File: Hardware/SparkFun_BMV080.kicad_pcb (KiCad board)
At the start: 2 copper layers, 24.1 x 12.7 mm, 54 parts, among them J1 Qwiic_RA, J2 Conn_01x07, U1 BMV080

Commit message: Changed C5 from DNP to populated
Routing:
- net 3.3V: track 48.2 -> 47.7 mm
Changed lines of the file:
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@@
 		)
 		(group ""
-			(members "0323bbcb-9db1-4550-bdcf-c58307372e8a" "129c8a7c-96b1-4d77-be27-7c0a68eae82b"
-				"17066dd4-91f0-4b2c-90e9-9da69e5faaa6" "1943d318-2756-45dc-b198-7f49738af2c3"
-				"3f605292-b843-4d37-babf-3784242fe08f" "4f4c8642-4329-4bf1-b3ef-893e8dab323c"
-				"57365592-8080-47cf-8e00-2132c18cfec5" "5d47b60e-56bd-45d7-bb0d-a27f9c249cd9"
-				"7191a7ac-3cfd-46b6-b47c-109da5e373e4" "743e579a-8922-4b10-a70a-2bff2a61b4e9"
-				"8350fa8f-af59-4aa9-b07d-7af58feef8e6" "99e0e99d-677b-4fb4-b25c-acb5b0a82601"
-				"9f4f398a-88a8-47ff-bd15-fe353347f26e" "adeaf1fb-c8a8-495c-b3dc-061e1177fc19"
-				"c20d4249-b260-447a-a5e6-acf935c38c30" "cd680a11-ecdf-470c-832d-11c97486f1ce"
-				"d777cdd7-b0db-4b6c-9eb7-9efd6433ac26" "e269340a-8f81-4c65-8b68-691e03761d3e"
-				"f43b7801-056e-4cbc-bdcf-bace62f3a128" "f48c44af-afb6-4a1e-9611-99fc4c60bd91"
-				"f6a77c4c-a699-4998-b09a-588a7a439803" "f8e37a14-ad18-4cdf-afa0-56f7ebb95e30"
-				"f9167eab-9848-4063-82ef-cf8f1aa0283d" "fe6070ae-ec9c-4269-b79c-fb7439431384"
+			(members "0ceba5bc-189c-4eae-8833-ca9dbc079d37" "1f663b43-5c1f-47e9-9c2b-0e138af4ceb2"
+				"35ecef30-701a-4ae0-abb4-b91e4a9bb35f" "4c3070f8-7595-4885-a99a-a6facd63b4d7"
+				"5acd4afe-5e46-4f77-8c4f-4d508bdab7df" "61c7252d-1063-4566-999f-4fc0c4eafa67"
+				"6407c94d-d9f4-4163-83dc-a27446e726f8" "711f668a-bbce-4460-92d5-2e2cb9263932"
+				"86f05a87-cb46-4ce1-99ac-246c7caf3355" "993f312a-53b4-4398-a6b3-1f8ffd14df01"
+				"ae4bcca0-e3f6-4d88-8f8d-e36f1c271b57" "ae4bce81-2b73-4186-9c70-5910d9db9cd7"
+				"af736b6d-5ec5-45a8-b9f0-5d125bc51396" "b1867b9a-aa29-47b2-84da-97c96f2a49b8"
+				"b66097e4-f0a4-4951-b7fc-f9bdb9b19a9e" "c71cbb7c-1523-4b6d-8205-3119d83c7f20"
+				"dcffac79-e62a-421f-9400-1164a284a8d9" "e88fcd85-46ed-4386-a12e-f83662d1dc38"
+				"ecad0877-a816-471d-b628-6088fbfe1e93" "f0717b40-129c-4219-b55f-f7d5f907be79"
+				"f15de511-9ecc-4bba-8d54-4c130d252e85" "f48ce54b-3d15-48d6-96cb-7c2bb2d5acba"
+				"f602eccc-5aa0-4869-a675-a465a2e67a34" "f780c958-a8ac-4002-8a30-fe8cb3588660"
 			)
 		)
 		(group ""
-			(members "3720748d-96f4-44c1-930f-83de2de9e6e6" "3f3fba18-211e-41a3-ba51-976b2923ebd1"
-				"48b4bfa4-e4f8-4cee-8010-c9c6888a8f20" "4ed068ba-5eca-41cd-886a-1229b8814574"
-				"542eba73-4fbb-468b-acee-2bdb3667f254" "6734b2cc-4870-4695-8d09-9d5a7687712e"
-				"6bd0c4f7-2192-41be-8adc-e0c41a3e553a" "93fcdc44-fb1b-4a33-b65b-43d007b5f669"
-				"9548979e-7292-4bed-8904-9b678ba7e0bb" "a480d734-605c-46e8-9c6a-b63f6f2b9b0b"
-				"aa4fac25-a87d-4ceb-99bc-9275ae9cb340" "bcd9040b-70e0-4c06-96e3-043c244d4851"
-				"de0a1da5-8957-4ae4-a6fe-f0af63f92c79" "f6420fb9-895e-4033-a284-81064fd5bd43"
+			(members "0335be06-102d-4263-bab1-12667eda6e8b" "38c72f74-21d1-425c-b6e8-509a0f78b6f3"
+				"3e9c3e0c-8359-4605-b76b-e8b7b21f3528" "505c8171-6575-45b8-8b41-329f054488d6"
+				"67fac45c-d807-45a9-bd04-f7a23e01c00d" "899ac419-171b-4f1c-b566-96660c695bdc"
+				"a2e41c72-f8ca-4b1a-82d9-f3002f2ddce2" "a6349dca-2aff-4e1a-b036-bd771e3eb8f8"
+				"bf23a2b1-279c-4095-b615-8f9de98552e9" "d26edaaf-7e9e-4d26-a137-f035ce0b2bc4"
+				"d627d596-f0cd-4127-9f8a-afefe62d29bf" "e23e056e-79b9-4709-94fd-23d215b02856"
+				"e99c97d1-8692-4be9-aaab-415d2e226c84" "fa415e96-26ef-4dcb-bd23-2b3b71b8cb64"
 			)
 		)
 		(model "${KIPRJMOD}/BMV080.3dshapes/BMV080_Sensor_and_FPC_Connector.step"
 			(offset
-				(xyz -0.35 -23.2 2)
+				(xyz -0.35 -23.15 1.97)
 			)
 			(scale
@@
 		(tags "SparkFun capacitor")
 		(property "Reference" "C5"
-			(at 0 1.43 90)
+			(at 0 1.43 -90)
 			(layer "B.Fab")
 			(effects
@@
 		)
 		(property "Value" "10uF"
-			(at 0 -1.43 90)
+			(at 0 -1.43 -90)
 			(layer "B.Fab")
 			(effects
@@
 		(sheetname "Root")
 		(sheetfile "SparkFun_BMV080.kicad_sch")
-		(attr smd dnp)
-		(fp_line
-			(start 0.14058 -0.51)
-			(end -0.14058 -0.51)
-			(stroke
-				(width 0.12)
-				(type solid)
-			)
-			(layer "B.SilkS")
-		)
-		(fp_line
-			(start 0.14058 0.51)
-			(end -0.14058 0.51)
+		(attr smd)
+		(fp_rect
+			(start -1.337 0.598)
+			(end 1.336 -0.586)
 			(stroke
-				(width 0.12)
-				(type solid)
+				(width 0.1)
+				(type default)
 			)
+			(fill none)
 			(layer "B.SilkS")
 		)
@@
 		)
 		(height 11.43)
-		(gr_text "950 mils"
+		(gr_text "24.13 mm"
 			(at 128.905 77.59 0)
 			(layer "Dwgs.User")
@@
 		)
 		(height -8.94)
-		(gr_text "500.00 mils"
+		(gr_text "12.70 mm"
 			(at 107.77 106.58 90)
 			(layer "Dwgs.User")
@@
 		)
 		(height 2.53)
-		(gr_text "60 mils"
+		(gr_text "1.52 mm"
 			(at 144.73 88.82 90)
 			(layer "Dwgs.User")
@@
 		)
 		(height 12.17)
-		(gr_text "179.921 mils"
+		(gr_text "4.57 mm"
 			(at 152.146 90.678 90)
 			(layer "Dwgs.User")
@@
 		(height -6.785)
 		(orientation 1)
-		(gr_text "75.000 mils"
+		(gr_text "1.905 mm"
 			(at 114.42 106.93 90)
 			(layer "Dwgs.User")
@@
 		(height 6.77)
 		(orientation 1)
-		(gr_text "171.1417 mils"
+		(gr_text "4.3470 mm"
 			(at 147.8 85.53 90)
 			(layer "Dwgs.User")
@@
 		(height 4.145)
 		(orientation 0)
-		(gr_text "100.2 mils"
+		(gr_text "2.5 mm"
 			(at 127.15 105.22 0)
 			(layer "Dwgs.User")
@@
 		(height -10.61)
 		(orientation 1)
-		(gr_text "250.00 mils"
+		(gr_text "6.35 mm"
 			(at 111.31 106.39 90)
 			(layer "Dwgs.User")
@@
 		(height 9.99)
 		(orientation 0)
-		(gr_text "175.000 mils"
+		(gr_text "4.445 mm"
 			(at 125.02 112.85 0)
 			(layer "Dwgs.User")
@@
 		(height 10.22)
 		(orientation 0)
-		(gr_text "175.197 mils"
+		(gr_text "4.450 mm"
 			(at 144.88 112.98 0)
 			(layer "Dwgs.User")
@@
 		(height -7.874)
 		(orientation 0)
-		(gr_text "912.2 mils"
+		(gr_text "23.17 mm"
 			(at 128.425 81.146 0)
 			(layer "Dwgs.User")
@@
 		(height -8.927)
 		(orientation 0)
-		(gr_text "124.843 mils"
+		(gr_text "3.171 mm"
 			(at 133.49 85.41 0)
 			(layer "Dwgs.User")
@@
 	)
 	(segment
-		(start 130.81 101.6)
-		(end 130.81 101.05)
-		(width 0.2032)
-		(layer "F.Cu")
-		(net 10)
-	)
-	(segment
 		(start 119.285 94.28)
 		(end 118.32 94.28)
@@
 		(min_thickness 0.254)
 		(filled_areas_thickness no)
-		(fill
+		(fill yes
 			(thermal_gap 0.3048)
 			(thermal_bridge_width 0.3048)

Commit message: ordering instructions updated to RED
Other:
- board text added: "Solder Mask: Red"
- board text removed: "Solder Mask: Black"
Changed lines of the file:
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@@
 		)
 	)
-	(gr_text "Solder Mask: Black"
+	(gr_text "Solder Mask: Red"
 		(at 220.3 172.32 0)
 		(layer "F.Fab")

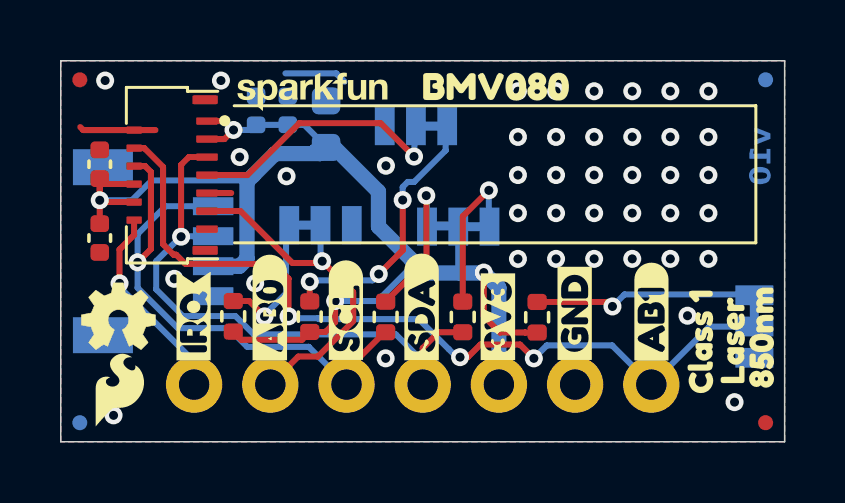
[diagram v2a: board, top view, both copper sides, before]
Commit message: library work
-moved bmv080 sensor symbol and footprint to sparkfun libraries with pending PR.
-updated symbol and footprints in kicad design files
-note, the sensor itself and the FPC connector are now separate things. The BMV080 has an "outline" footprint that is placed at the same origin point as the sensor (and includes the 3d model of the sensor itself)
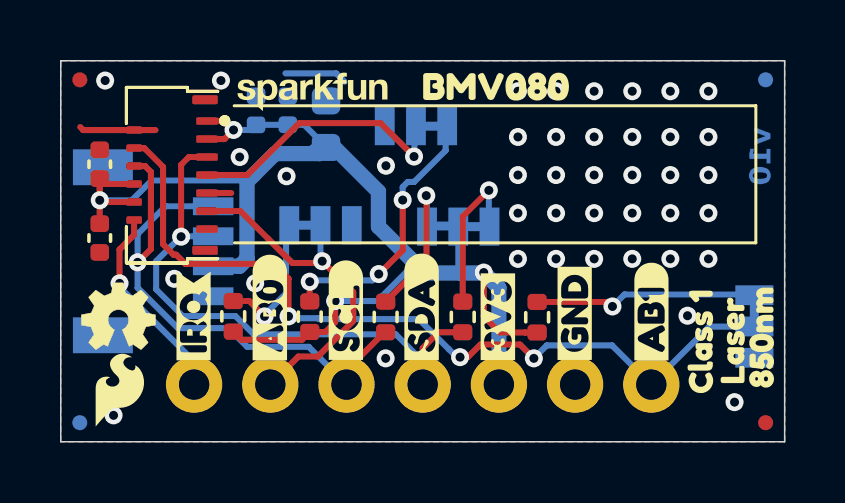
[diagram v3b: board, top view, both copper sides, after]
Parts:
- added REF**: BMV080_Outline, SparkFun-Sensor:BMV080_Outline, F.Cu at (120.5, 94.0)
- U1: footprint BMV080:FPC_0.3mm-13_molex_503566-1302 -> SparkFun-Connector:FPC_0.3mm-13

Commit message: Update STEP file
-step file now includes the 3d model of the sensor
-also updated some library work around the FPC and sensor step files
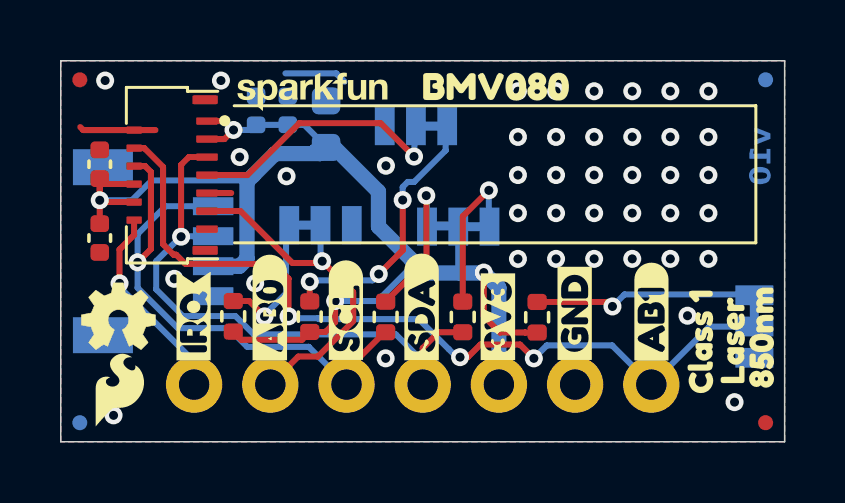
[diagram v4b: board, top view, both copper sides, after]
